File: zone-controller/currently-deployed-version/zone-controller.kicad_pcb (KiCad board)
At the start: 2 copper layers, 190 x 153.2 mm, 1010 parts, among them J1 EBBA-02-C-SS-BU, J10 EBBA-02-C-SS-BU, J11 EBBA-02-C-SS-BU, J12 EBBA-02-C-SS-BU, J13 EBBA-02-C-SS-BU, J14 EBBA-02-C-SS-BU, J15 EBBA-02-C-SS-BU, J16 1x4_idc_lsa, J17 54601-908WPLF, J18 1x4_idc_lsa, J19 EBBA-02-C-SS-BU, J2 EBBA-02-C-SS-BU, J3 EBBA-02-C-SS-BU, J4 EBBA-02-C-SS-BU, J5 EBBA-02-C-SS-BU, J6 EBBA-02-C-SS-BU, J7 EBBA-02-C-SS-BU, J8 EBBA-02-C-SS-BU, J9 EBBA-02-C-SS-BU, P1 1x3_pin_header, P10 1x2_pin_header, P11 1x2_pin_header, P12 1x2_pin_header, P13 1x2_pin_header, P14 1x2_pin_header, P15 1x2_pin_header, P16 1x2_pin_header, P2 1x3_pin_header, P3 1x3_pin_header, P4 1x3_pin_header, P5 1x3_pin_header, P6 1x3_pin_header, P7 1x2_pin_header, P8 1x2_pin_header, P9 1x2_pin_header, Q1 AOD458, Q10 AOD458, Q11 AOD458, Q12 AOD458, Q13 PMV213SN,215, Q14 PMV213SN,215, Q15 AOB1608L, Q17 AOB1608L, Q18 PMV213SN,215, Q19 PMV213SN,215, Q2 AOD458, Q20 AOB1608L, Q21 AOB1608L, Q22 PMV213SN,215, Q23 PMV213SN,215, Q3 AOD458, Q4 AOD458, Q5 AOD458, Q6 AOD458, Q7 AOD458, Q8 AOD458, Q9 AOD458, SW1 SMTS-102-2C2T, SW10 SMTS-102-2C2T, SW11 SMTS-102-2C2T, SW12 SMTS-102-2C2T, SW13 SMTS-102-2C2T, SW2 SMTS-102-2C2T, SW3 SMTS-102-2C2T, SW4 SMTS-102-2C2T, SW5 SMTS-102-2C2T, SW6 SMTS-102-2C2T, SW7 SMTS-102-2C2T, SW8 SMTS-102-2C2T, SW9 SMTS-102-2C2T, U1 TLP2345, U10 TLP2345, U11 TLP2345, U12 TLP2345, U13 TLP2345, U14 TLP2345, U15 TLP2345, U16 TLP2345, U17 TLP2345, U18 TLP2345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

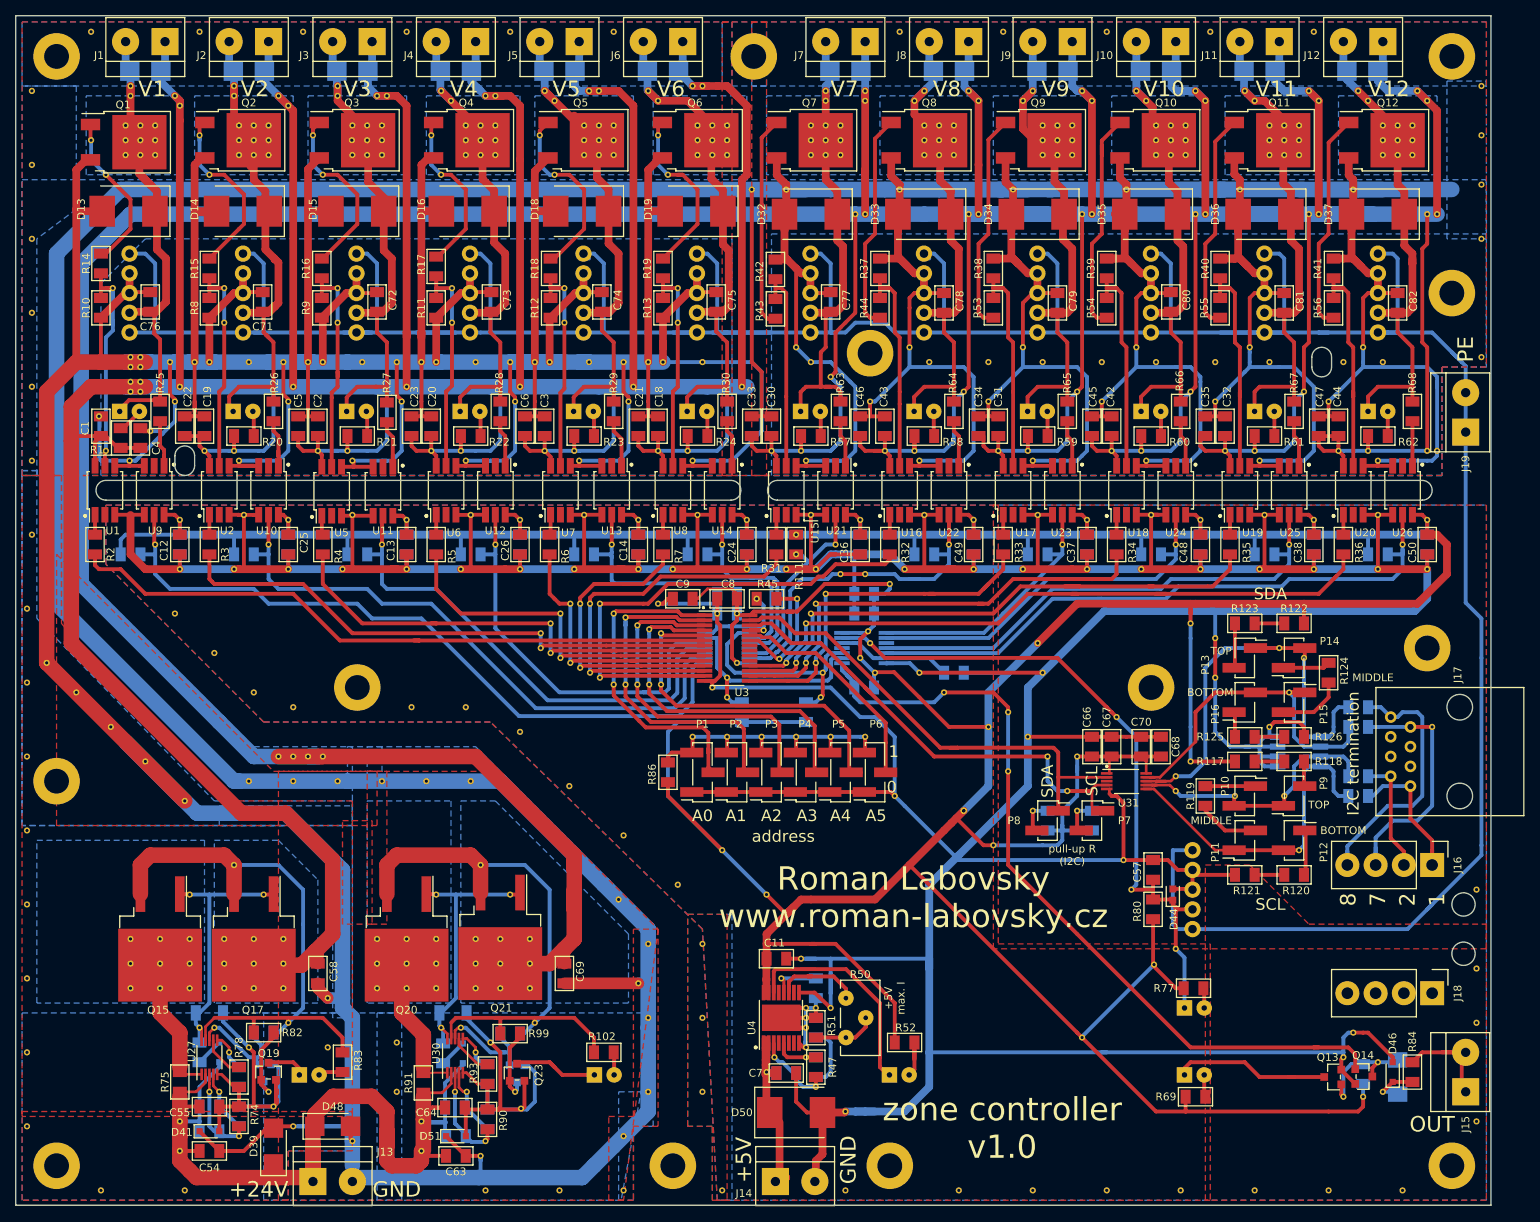
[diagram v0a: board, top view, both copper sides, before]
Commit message: Split project to sheets and adding of description about project.
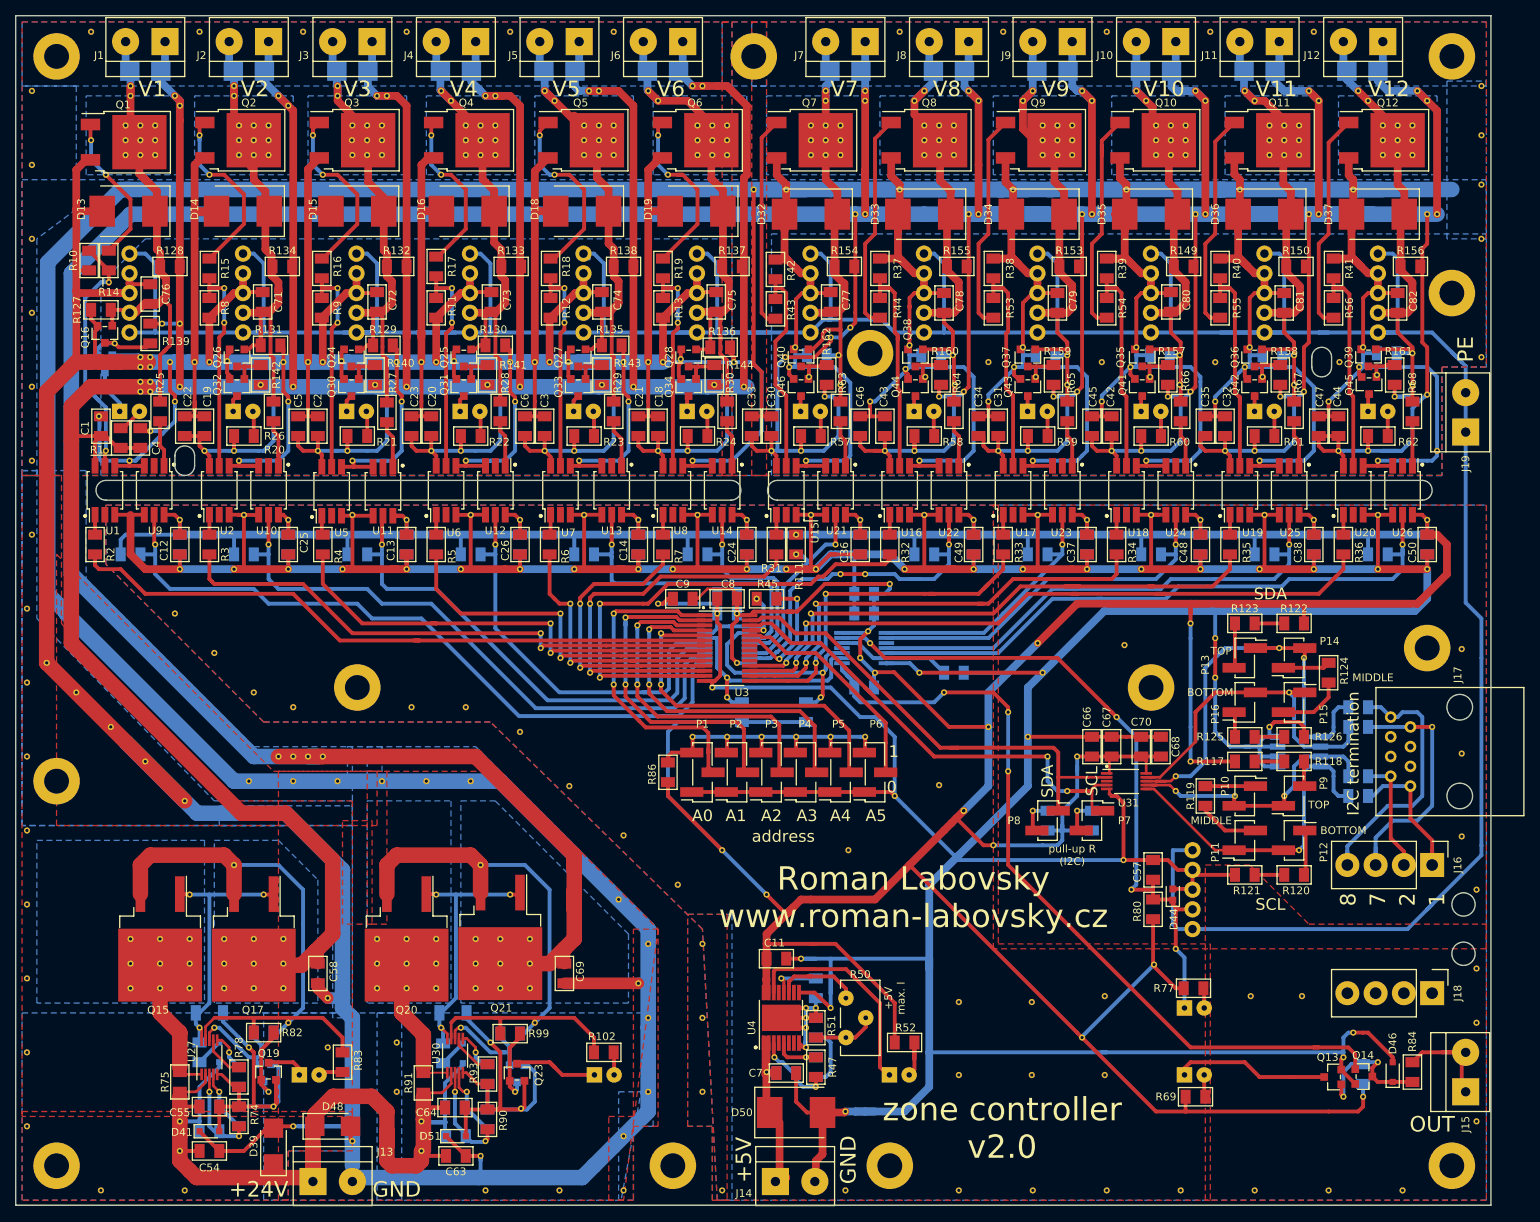
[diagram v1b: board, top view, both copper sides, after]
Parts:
- removed D47: PMEG40T30EPX, package_sod_rl:sod_128
- removed the ~ at (118.1, 36.2)
- removed the ~ at (103.5, 36.2)
- removed the ~ at (88.9, 36.2)
- removed the ~ at (74.3, 36.2)
- removed the ~ at (59.7, 36.2)
- removed the ~ at (205.7, 130.2)
- removed the ~ at (132.1, 36.2)
- removed the ~ at (205.7, 36.2)
- removed the ~ at (191.1, 36.2)
- removed the ~ at (176.5, 36.2)
- removed the ~ at (161.9, 36.2)
- removed the ~ at (147.3, 36.2)
- removed the ~ at (211.5, 47.6)
- removed the ~ at (134.6, 38.1)
- removed the ~ at (124.5, 14.0)
- added Q16: 2N7002A-YAN, package_sot_rl:sot_23, F.Cu at (41.1, 32.5)
- added Q24: 2N7002A-YAN, package_sot_rl:sot_23, F.Cu at (72.9, 35.6)
- added Q25: 2N7002A-YAN, package_sot_rl:sot_23, F.Cu at (87.4, 35.6)
- added Q26: 2N7002A-YAN, package_sot_rl:sot_23, F.Cu at (58.2, 35.6)
- added Q27: 2N7002A-YAN, package_sot_rl:sot_23, F.Cu at (102.1, 35.6)
- added Q28: 2N7002A-YAN, package_sot_rl:sot_23, F.Cu at (116.3, 35.6)
- added Q29: 2N7002A-YAN, package_sot_rl:sot_23, B.Cu at (41.1, 36.3)
- added Q30: 2N7002A-YAN, package_sot_rl:sot_23, F.Cu at (72.9, 39.4)
- added Q31: 2N7002A-YAN, package_sot_rl:sot_23, F.Cu at (87.4, 39.4)
- added Q32: 2N7002A-YAN, package_sot_rl:sot_23, F.Cu at (58.2, 39.4)
- added Q33: 2N7002A-YAN, package_sot_rl:sot_23, F.Cu at (102.1, 39.4)
- added Q34: 2N7002A-YAN, package_sot_rl:sot_23, F.Cu at (116.3, 39.4)
- added Q35: 2N7002A-YAN, package_sot_rl:sot_23, F.Cu at (174.8, 35.5)
- added Q36: 2N7002A-YAN, package_sot_rl:sot_23, F.Cu at (189.2, 35.6)
- added Q37: 2N7002A-YAN, package_sot_rl:sot_23, F.Cu at (160.0, 35.6)
- added Q38: 2N7002A-YAN, package_sot_rl:sot_23, F.Cu at (145.5, 35.6)
- added Q39: 2N7002A-YAN, package_sot_rl:sot_23, F.Cu at (203.9, 35.5)
- added Q40: 2N7002A-YAN, package_sot_rl:sot_23, F.Cu at (130.8, 35.5)
- added Q41: 2N7002A-YAN, package_sot_rl:sot_23, F.Cu at (174.8, 39.4)
- added Q42: 2N7002A-YAN, package_sot_rl:sot_23, F.Cu at (189.2, 39.4)
- added Q43: 2N7002A-YAN, package_sot_rl:sot_23, F.Cu at (160.0, 39.4)
- added Q44: 2N7002A-YAN, package_sot_rl:sot_23, F.Cu at (145.5, 39.4)
- added Q45: 2N7002A-YAN, package_sot_rl:sot_23, F.Cu at (204.0, 39.1)
- added Q46: 2N7002A-YAN, package_sot_rl:sot_23, F.Cu at (130.8, 39.4)
- added R127: 10k, resistor_smd_rl:r_1206, F.Cu at (40.6, 29.5)
- added R128: 2k2/0.5W, resistor_smd_rl:r_1206, F.Cu at (49.5, 23.9)
- added R129: 10k, resistor_smd_rl:r_1206, F.Cu at (77.0, 34.0)
- added R130: 10k, resistor_smd_rl:r_1206, F.Cu at (91.4, 34.0)
- added R131: 10k, resistor_smd_rl:r_1206, F.Cu at (62.5, 34.0)
- added R132: 2k2/0.5W, resistor_smd_rl:r_1206, F.Cu at (78.7, 23.9)
- added R133: 2k2/0.5W, resistor_smd_rl:r_1206, F.Cu at (93.5, 23.9)
- added R134: 2k2/0.5W, resistor_smd_rl:r_1206, F.Cu at (64.0, 23.9)
- added R135: 10k, resistor_smd_rl:r_1206, F.Cu at (106.4, 34.0)
- added R136: 10k, resistor_smd_rl:r_1206, F.Cu at (120.4, 34.3)
- added R137: 2k2/0.5W, resistor_smd_rl:r_1206, F.Cu at (121.9, 23.9)
- added R138: 2k2/0.5W, resistor_smd_rl:r_1206, F.Cu at (108.0, 23.9)
- added R139: 10k, resistor_smd_rl:r_1206, F.Cu at (47.0, 32.5)
- added R140: 10k, resistor_smd_rl:r_1206, F.Cu at (75.9, 37.8)
- added R141: 10k, resistor_smd_rl:r_1206, F.Cu at (90.4, 37.8)
- added R142: 10k, resistor_smd_rl:r_1206, F.Cu at (61.2, 37.8)
- added R143: 10k, resistor_smd_rl:r_1206, F.Cu at (105.2, 37.8)
- added R144: 10k, resistor_smd_rl:r_1206, F.Cu at (119.6, 37.8)
- added R145: 10k, resistor_smd_rl:r_1206, B.Cu at (177.0, 35.3)
- added R146: 10k, resistor_smd_rl:r_1206, B.Cu at (191.5, 35.3)
- added R147: 10k, resistor_smd_rl:r_1206, B.Cu at (162.3, 35.3)
- added R148: 10k, resistor_smd_rl:r_1206, B.Cu at (147.6, 35.3)
- added R149: 2k2/0.5W, resistor_smd_rl:r_1206, F.Cu at (180.1, 23.9)
- added R150: 2k2/0.5W, resistor_smd_rl:r_1206, F.Cu at (194.6, 23.9)
- added R151: 10k, resistor_smd_rl:r_1206, B.Cu at (206.2, 35.1)
- added R152: 10k, resistor_smd_rl:r_1206, B.Cu at (132.8, 35.3)
- added R153: 2k2/0.5W, resistor_smd_rl:r_1206, F.Cu at (165.4, 23.9)
- added R154: 2k2/0.5W, resistor_smd_rl:r_1206, F.Cu at (136.4, 23.9)
- added R155: 2k2/0.5W, resistor_smd_rl:r_1206, F.Cu at (150.9, 23.9)
- added R156: 2k2/0.5W, resistor_smd_rl:r_1206, F.Cu at (209.3, 23.9)
- added R157: 10k, resistor_smd_rl:r_1206, F.Cu at (178.1, 37.8)
- added R158: 10k, resistor_smd_rl:r_1206, F.Cu at (192.5, 37.8)
- added R159: 10k, resistor_smd_rl:r_1206, F.Cu at (163.3, 37.8)
- added R160: 10k, resistor_smd_rl:r_1206, F.Cu at (148.8, 37.8)
- added R161: 10k, resistor_smd_rl:r_1206, F.Cu at (207.3, 37.8)
- added R162: 10k, resistor_smd_rl:r_1206, F.Cu at (134.1, 37.8)
- added ~: ~, via_pad_rl:via_pad_0.4x0.8, F.Cu at (172.5, 72.6)
- added ~: ~, via_pad_rl:via_pad_0.4x0.8, F.Cu at (151.1, 118.6)
- added ~: ~, via_pad_rl:via_pad_0.4x0.8, F.Cu at (160.5, 128.0)
- added ~: ~, via_pad_rl:via_pad_0.4x0.8, F.Cu at (215.9, 73.2)
- added ~: ~, via_pad_rl:via_pad_0.4x0.8, F.Cu at (215.9, 86.6)
- added ~: ~, via_pad_rl:via_pad_0.4x0.8, F.Cu at (215.9, 97.3)
- added ~: ~, via_pad_rl:via_pad_0,4x0,8, F.Cu at (42.4, 33.8)
- added ~: ~, via_pad_rl:via_pad_0,4x0,8, F.Cu at (202.7, 36.8)
- added ~: ~, via_pad_rl:via_pad_0,4x0,8, F.Cu at (209.6, 35.1)
- added ~: ~, via_pad_rl:via_pad_0,4x0,8, F.Cu at (205.0, 37.8)
- added ~: ~, via_pad_rl:via_pad_0.4x0.8, F.Cu at (195.3, 117.9)
- added ~: ~, via_pad_rl:via_pad_0,4x0,8, F.Cu at (209.6, 39.1)
- added ~: ~, via_pad_rl:via_pad_0,4x0,8, F.Cu at (211.5, 40.4)
- added ~: ~, via_pad_rl:via_pad_0,4x0,8, F.Cu at (207.3, 40.6)
- added ~: ~, via_pad_rl:via_pad_0,4x0,8, F.Cu at (194.3, 35.3)
- added ~: ~, via_pad_rl:via_pad_0,4x0,8, F.Cu at (190.2, 38.1)
- added ~: ~, via_pad_rl:via_pad_0,4x0,8, F.Cu at (192.5, 40.6)
- added ~: ~, via_pad_rl:via_pad_0,4x0,8, F.Cu at (194.3, 39.1)
- added ~: ~, via_pad_rl:via_pad_0,4x0,8, F.Cu at (188.0, 36.8)
- added ~: ~, via_pad_rl:via_pad_0,4x0,8, F.Cu at (179.6, 35.3)
- added ~: ~, via_pad_rl:via_pad_0,4x0,8, F.Cu at (179.6, 39.1)
- added ~: ~, via_pad_rl:via_pad_0.4x0.8, F.Cu at (169.9, 117.9)
- added ~: ~, via_pad_rl:via_pad_0,4x0,8, F.Cu at (175.8, 38.1)
- added ~: ~, via_pad_rl:via_pad_0,4x0,8, F.Cu at (173.2, 36.8)
- added ~: ~, via_pad_rl:via_pad_0,4x0,8, F.Cu at (178.1, 40.6)
- added ~: ~, via_pad_rl:via_pad_0,4x0,8, F.Cu at (133.9, 40.6)
- added ~: ~, via_pad_rl:via_pad_0,4x0,8, F.Cu at (134.6, 33.0)
- added ~: ~, via_pad_rl:via_pad_0,4x0,8, F.Cu at (128.8, 35.6)
- added ~: ~, via_pad_rl:via_pad_0,4x0,8, F.Cu at (131.8, 38.1)
- added ~: ~, via_pad_rl:via_pad_0,4x0,8, F.Cu at (135.6, 35.3)
- added ~: ~, via_pad_rl:via_pad_0,4x0,8, F.Cu at (135.9, 39.1)
- added ~: ~, via_pad_rl:via_pad_0,4x0,8, F.Cu at (146.8, 38.1)
- added ~: ~, via_pad_rl:via_pad_0.4x0.8, F.Cu at (151.1, 128.0)
- added ~: ~, via_pad_rl:via_pad_0,4x0,8, F.Cu at (150.6, 39.1)
- added ~: ~, via_pad_rl:via_pad_0,4x0,8, F.Cu at (150.4, 35.3)
- added ~: ~, via_pad_rl:via_pad_0,4x0,8, F.Cu at (144.3, 37.1)
- added ~: ~, via_pad_rl:via_pad_0,4x0,8, F.Cu at (158.2, 36.8)
- added ~: ~, via_pad_rl:via_pad_0,4x0,8, F.Cu at (165.1, 35.3)
- added ~: ~, via_pad_rl:via_pad_0,4x0,8, F.Cu at (165.1, 39.1)
- added ~: ~, via_pad_rl:via_pad_0,4x0,8, F.Cu at (161.0, 38.1)
- added ~: ~, via_pad_rl:via_pad_0,4x0,8, F.Cu at (163.3, 40.6)
- added ~: ~, via_pad_rl:via_pad_0,4x0,8, F.Cu at (148.6, 40.6)
- added ~: ~, via_pad_rl:via_pad_0,4x0,8, F.Cu at (130.0, 34.3)
- added ~: ~, via_pad_rl:via_pad_0.4x0.8, F.Cu at (169.9, 128.0)
- added ~: ~, via_pad_rl:via_pad_0,4x0,8, F.Cu at (137.2, 31.8)
- added ~: ~, via_pad_rl:via_pad_0,4x0,8, F.Cu at (122.2, 36.2)
- added ~: ~, via_pad_rl:via_pad_0,4x0,8, F.Cu at (115.3, 35.8)
- added ~: ~, via_pad_rl:via_pad_0,4x0,8, F.Cu at (119.6, 39.1)
- added ~: ~, via_pad_rl:via_pad_0,4x0,8, F.Cu at (105.2, 39.1)
- added ~: ~, via_pad_rl:via_pad_0,4x0,8, F.Cu at (100.8, 36.2)
- added ~: ~, via_pad_rl:via_pad_0,4x0,8, F.Cu at (86.1, 36.1)
- added ~: ~, via_pad_rl:via_pad_0,4x0,8, F.Cu at (90.4, 39.1)
- added ~: ~, via_pad_rl:via_pad_0,4x0,8, F.Cu at (71.6, 36.1)
- added ~: ~, via_pad_rl:via_pad_0,4x0,8, F.Cu at (75.9, 39.1)
- added ~: ~, via_pad_rl:via_pad_0.4x0.8, F.Cu at (148.6, 90.7)
- added ~: ~, via_pad_rl:via_pad_0,4x0,8, F.Cu at (56.9, 36.1)
- added ~: ~, via_pad_rl:via_pad_0,4x0,8, F.Cu at (61.2, 39.1)
- added ~: ~, via_pad_rl:via_pad_0,4x0,8, F.Cu at (48.5, 31.2)
- added ~: ~, via_pad_rl:via_pad_0,4x0,8, F.Cu at (50.8, 31.2)
- added ~: ~, via_pad_rl:via_pad_0,4x0,8, F.Cu at (124.7, 14.0)
- added ~: ~, via_pad_rl:via_pad_0.4x0.8, F.Cu at (136.9, 99.1)
- added ~: ~, via_pad_rl:via_pad_0.4x0.8, F.Cu at (188.7, 117.9)
- added ~: ~, via_pad_rl:via_pad_0.4x0.8, F.Cu at (160.5, 118.6)
- R1, R102, R20, R21, R22, R23, R24, R57, R58, R59, R60, R61, R62, R83: value 2k2/0.5W -> 4k7
- R25: value 7k5 -> 4k7
- R72: value 1k -> 250R
- moved R10 6.28 mm to (39.1, 23.1)
- moved ~ 2.69 mm to (129.3, 36.8)
- moved ~ 1.27 mm to (47.0, 40.0)
- moved ~ 1.27 mm to (47.0, 36.8)
- moved ~ 1.27 mm to (47.0, 38.7)
- moved ~ 1.27 mm to (47.0, 35.6)
- moved ~ 1.27 mm to (45.7, 40.0)
- moved ~ 1.27 mm to (45.7, 36.8)
- moved ~ 1.27 mm to (45.7, 35.6)
- moved ~ 1.27 mm to (45.7, 38.7)
- moved R14 1.09 mm to (41.7, 23.1)
- moved C76 1.02 mm to (47.0, 27.4)
- moved ~ 0.92 mm to (41.7, 25.9)
- moved ~ 0.51 mm to (200.2, 36.2)
- moved ~ 0.25 mm to (123.4, 39.4)
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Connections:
- D1 pad 1: /LED0_24V -> Net-(D1-Pad1)
- D10 pad 1: /LED3_24V -> Net-(D10-Pad1)
- D11 pad 1: /LED4_24V -> Net-(D11-Pad1)
- D12 pad 1: /LED5_24V -> Net-(D12-Pad1)
- D26 pad 1: /LED6_24V -> Net-(D26-Pad1)
- D27 pad 1: /LED7_24V -> Net-(D27-Pad1)
- D28 pad 1: /LED8_24V -> Net-(D28-Pad1)
- D29 pad 1: /LED9_24V -> Net-(D29-Pad1)
- D30 pad 1: /LED10_24V -> Net-(D30-Pad1)
- D31 pad 1: /LED11_24V -> Net-(D31-Pad1)
- D46 pad 1: Net-(D46-Pad1) -> /PUMP_ACTIVE_0
- D8 pad 1: /LED1_24V -> Net-(D8-Pad1)
- D9 pad 1: /LED2_24V -> Net-(D9-Pad1)
- R84 pad 2: Net-(D46-Pad1) -> /PUMP_ACTIVE_0
- U4 pad 8: Net-(C10-Pad2) -> Net-(U4-Pad8)
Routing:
- net GND_A: track 1739.6 -> 1806.9 mm
- net +24V_B: track 832.6 -> 871.3 mm
- net Net-(Q16-Pad3): track 0.00 -> 9.64 mm
- net Net-(Q38-Pad3): track 0.00 -> 6.96 mm
- net Net-(D1-Pad1): track 0.00 -> 6.64 mm
- net Net-(Q36-Pad3): track 0.00 -> 6.47 mm
- net Net-(D46-Pad1): track 6.36 -> 0.00 mm
- net Net-(Q40-Pad3): track 0.00 -> 5.79 mm
- net Net-(Q35-Pad3): track 0.00 -> 5.46 mm
- net Net-(Q37-Pad3): track 0.00 -> 5.30 mm
- net Net-(Q26-Pad3): track 0.00 -> 5.28 mm
- net Net-(Q28-Pad3): track 0.00 -> 5.09 mm
- net Net-(Q39-Pad3): track 0.00 -> 5.02 mm
- net Net-(Q25-Pad3): track 0.00 -> 4.78 mm
- net Net-(Q24-Pad3): track 0.00 -> 4.74 mm
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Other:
- board text added: "zone controller v2.0"
- board text removed: "zone controller v1.0"
